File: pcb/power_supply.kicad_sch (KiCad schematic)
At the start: 47 parts, among them J101 TO_IO, U101 10M02SCE144, U102 74LVC2G17, U103 74LVC2G17, U104 74LVC2G17, U105 74LVC2G17

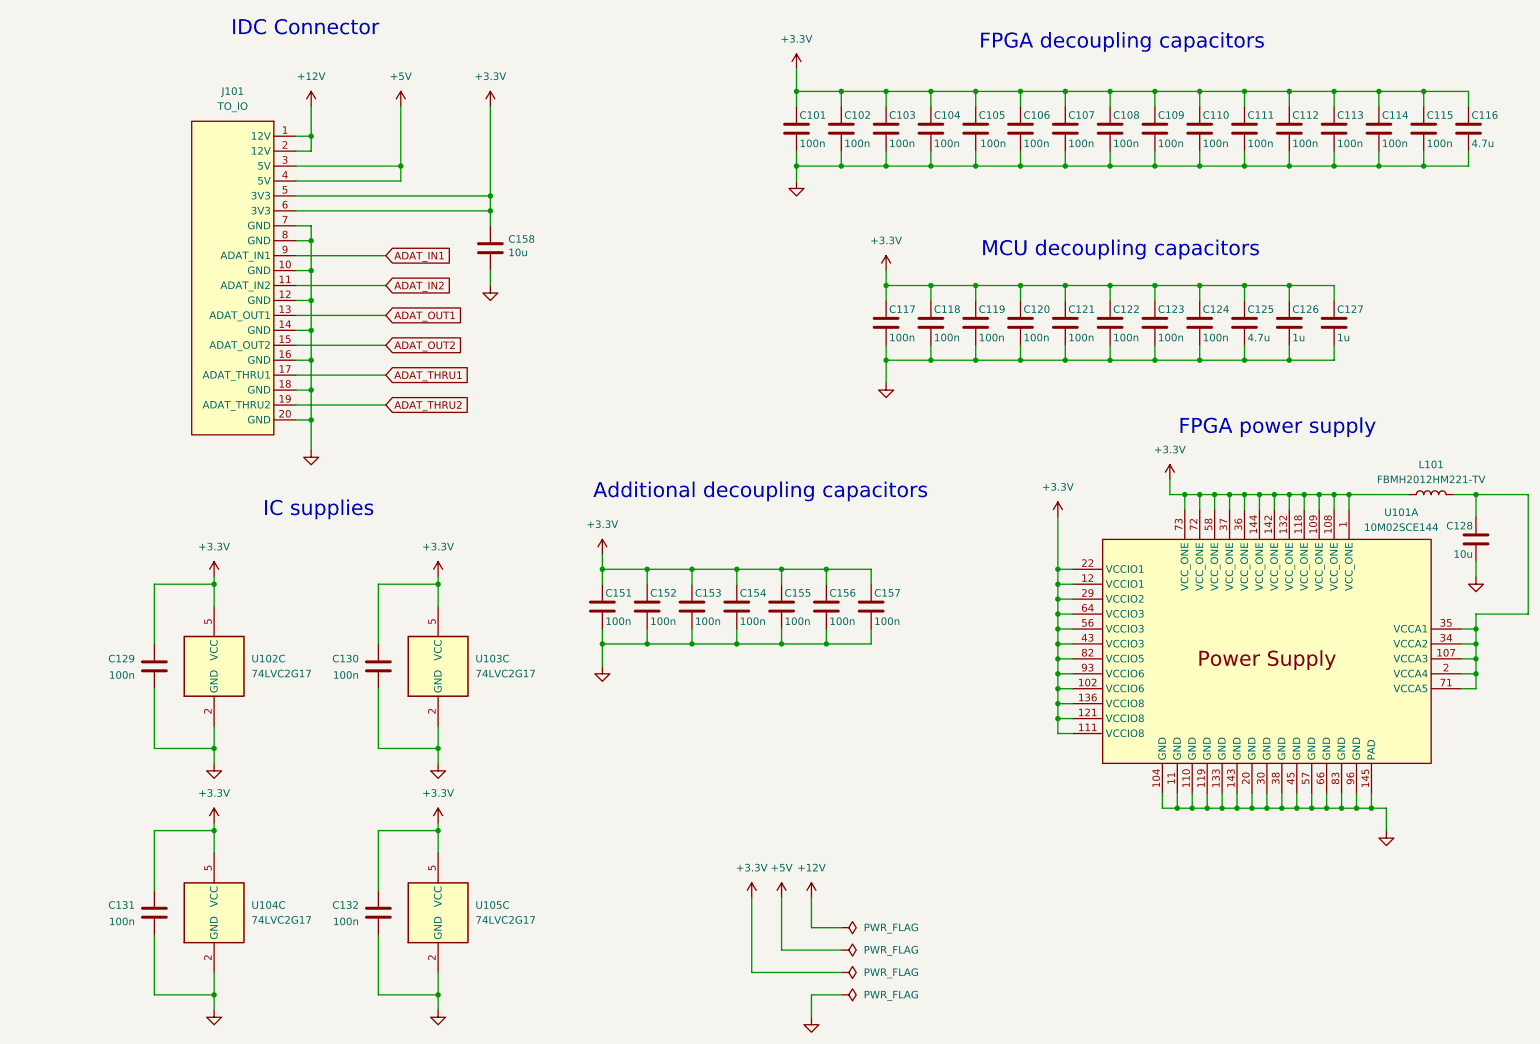
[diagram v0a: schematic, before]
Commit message: Add buffers for ADAT transfer
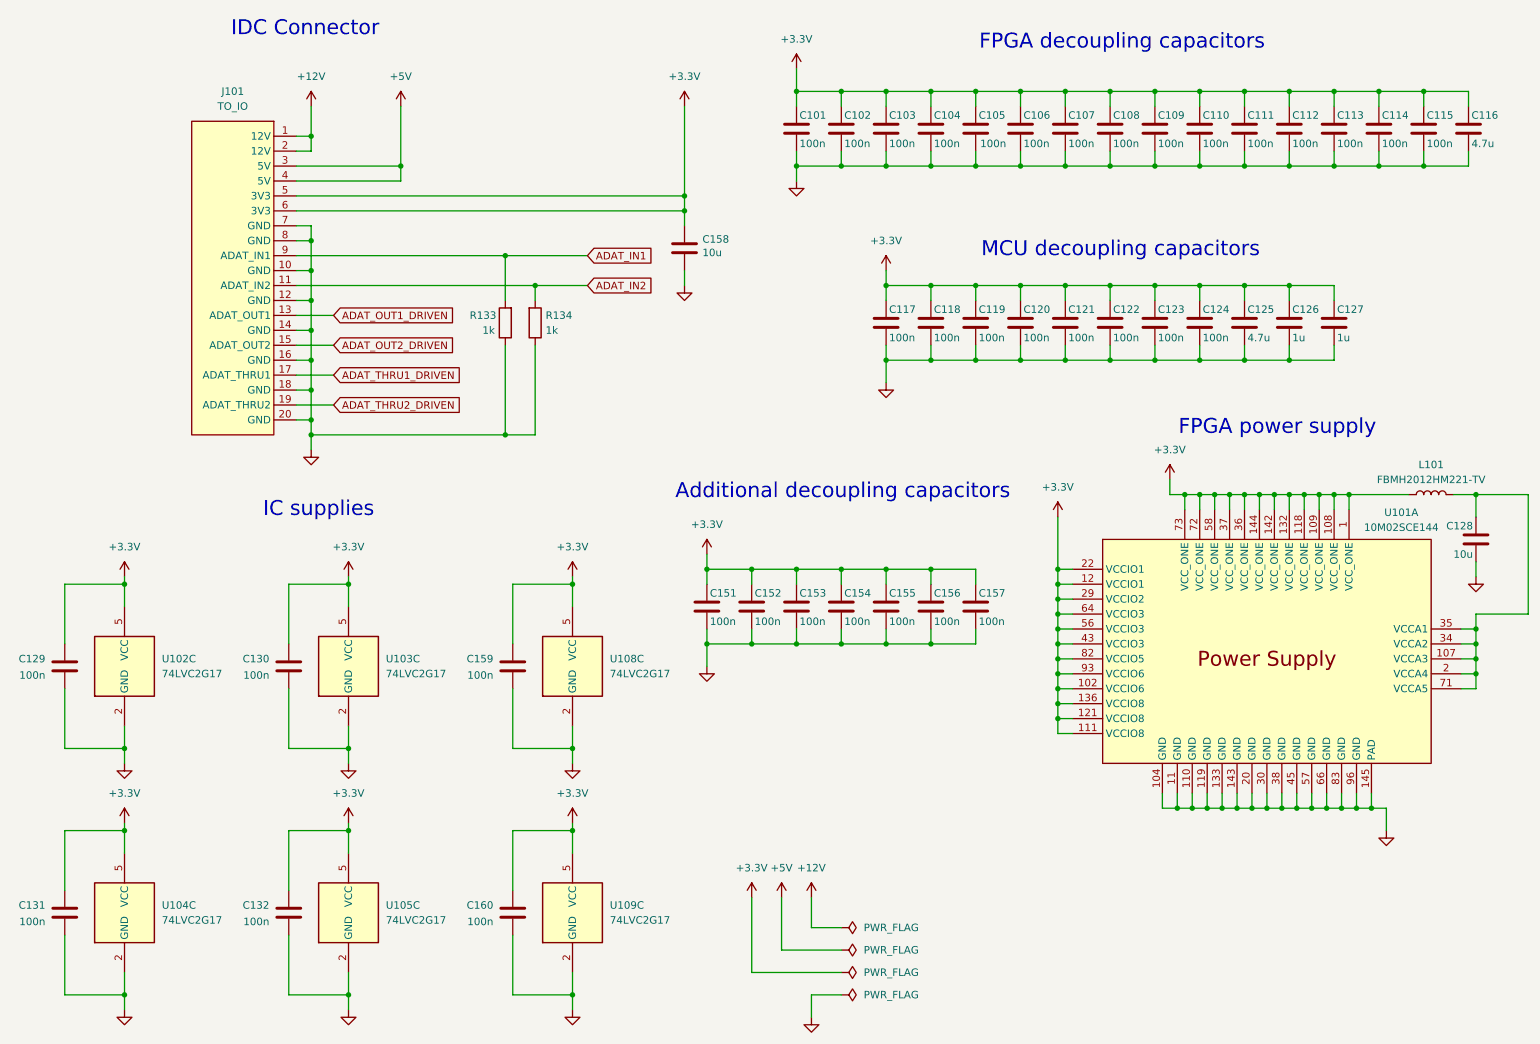
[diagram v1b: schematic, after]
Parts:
- added C159, C160: 100n, Capacitor_SMD:C_0805_2012Metric_Pad1.18x1.45mm_HandSolder, symbol Device:C
- added R133, R134: 1k, Resistor_SMD:R_0805_2012Metric_Pad1.20x1.40mm_HandSolder, symbol Device:R
- added U108, U109: 74LVC2G17, Package_TO_SOT_SMD:SOT-23-6_Handsoldering, symbol 74xGxx:74LVC2G17
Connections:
- net +3.3V: now also C159.1, C160.1, U108.5 (VCC), U109.5 (VCC)
- net ADAT_IN1: now also R133.2
- net ADAT_IN2: now also R134.2
- net GND: now also C159.2, C160.2, R133.1, R134.1, U108.2 (GND), U109.2 (GND)
- net ADAT_OUT1 renamed ADAT_OUT1_DRIVEN
- net ADAT_OUT2 renamed ADAT_OUT2_DRIVEN
- net ADAT_THRU1 renamed ADAT_THRU1_DRIVEN
- net ADAT_THRU2 renamed ADAT_THRU2_DRIVEN
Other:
- moved on the sheet: C129, C130, C131, C132, C151, C152, C153, C154, C155, C156, C157, C158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

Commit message: Assign FPGA pins, change MCU to STM32F429VET6
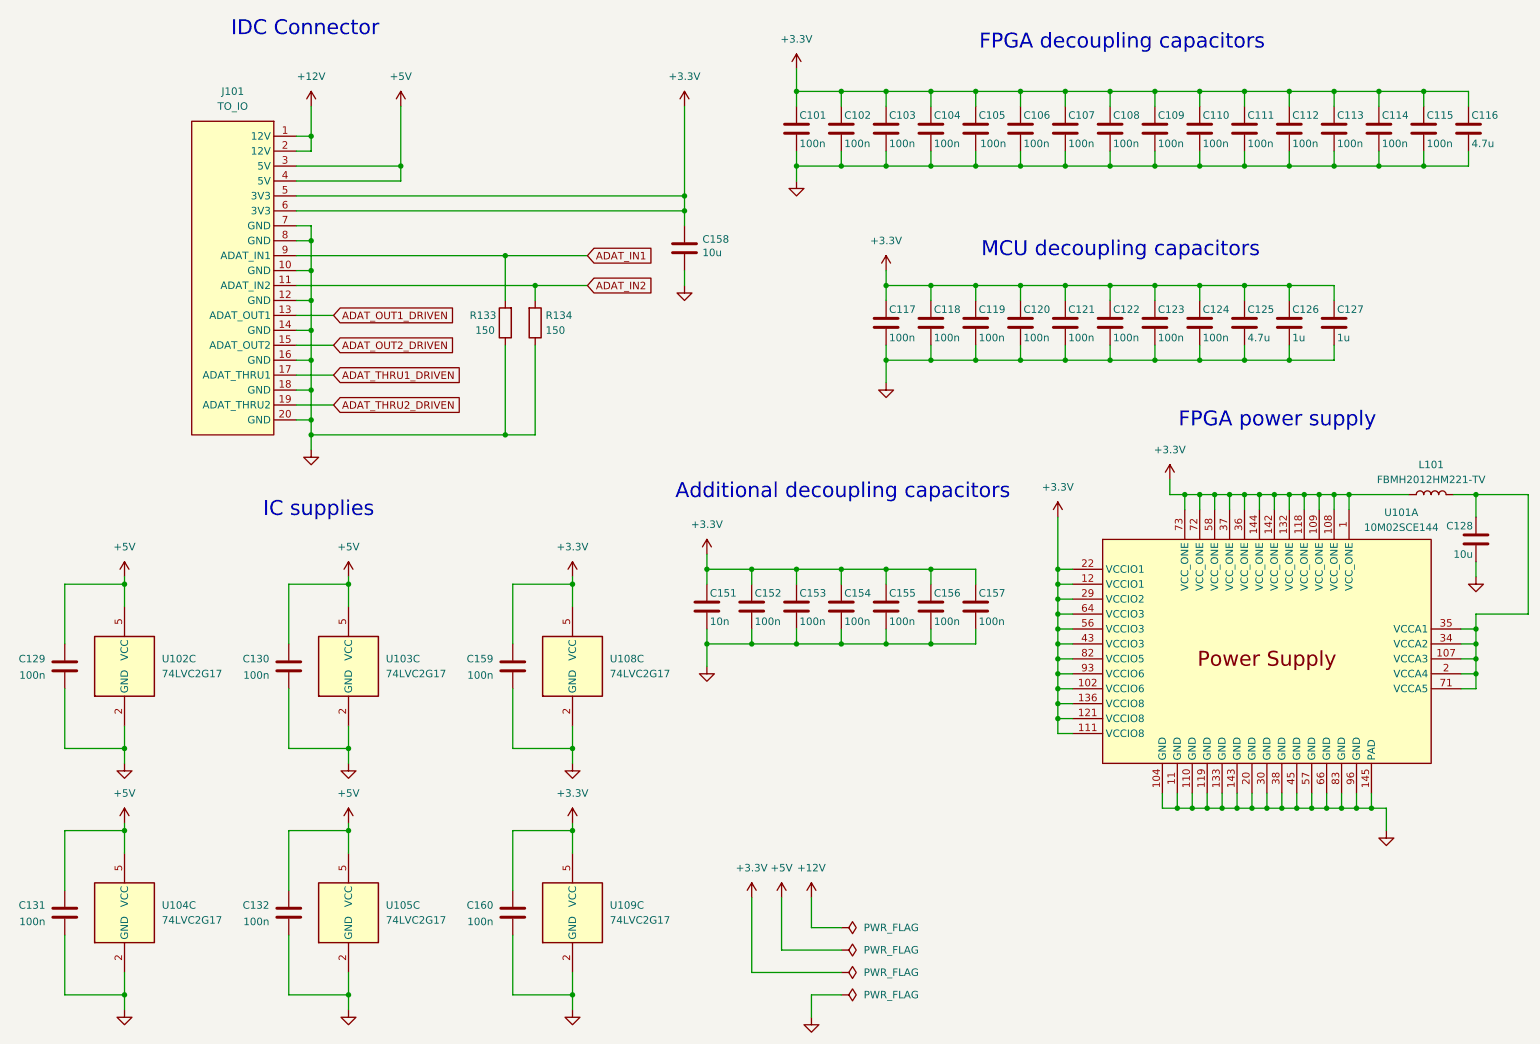
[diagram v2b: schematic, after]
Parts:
- C151: value 100n -> 10n
- R133, R134: value 1k -> 150
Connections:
- net +3.3V: no longer C129.1, C130.1, C131.1, C132.1, U102.5 (VCC), U103.5 (VCC), U104.5 (VCC), U105.5 (VCC)
- net +5V: now also C129.1, C130.1, C131.1, C132.1, U102.5 (VCC), U103.5 (VCC), U104.5 (VCC), U105.5 (VCC)
